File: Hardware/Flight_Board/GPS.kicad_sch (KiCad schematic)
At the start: 7 parts, among them U5 CAM-M8Q-0

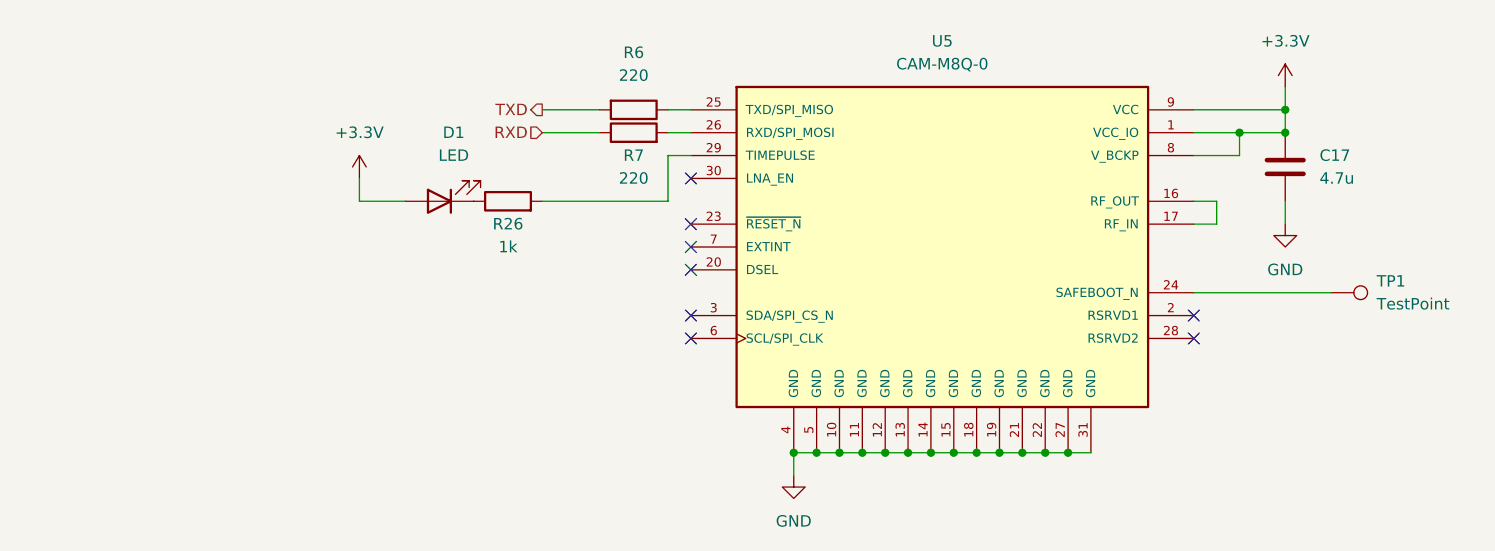
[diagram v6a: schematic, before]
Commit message: Add LEDs and test points
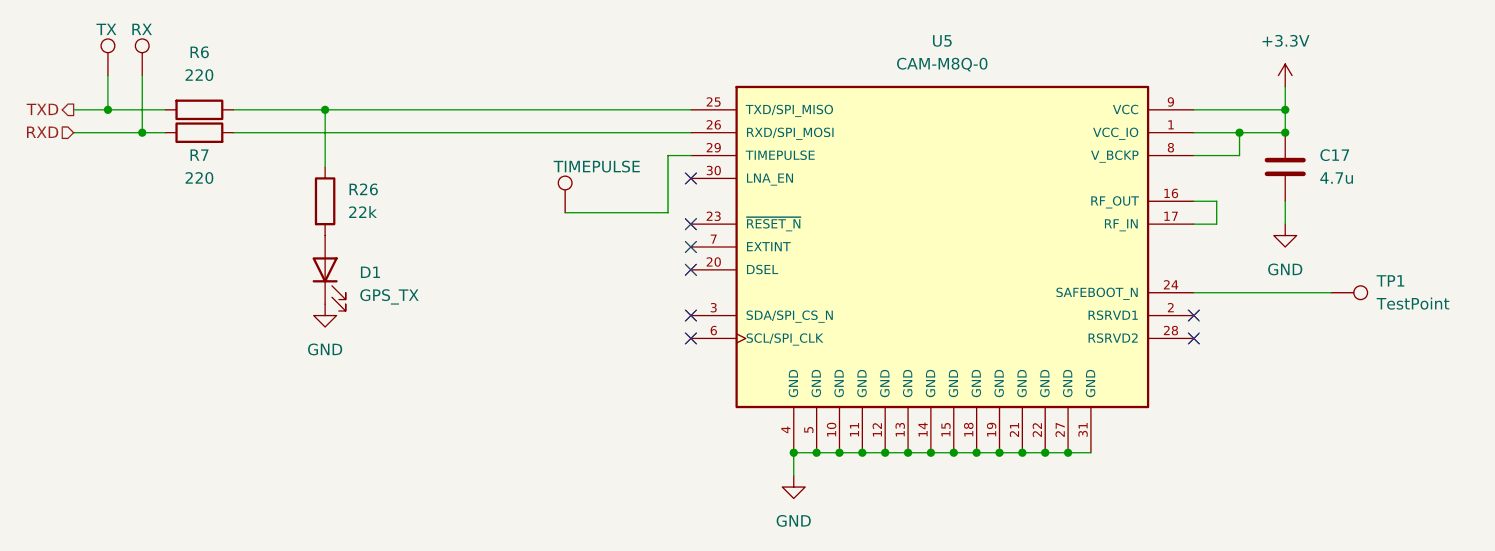
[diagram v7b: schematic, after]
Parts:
- added TP2: RX, symbol Connector:TestPoint
- added TP2: TIMEPULSE, symbol Connector:TestPoint
- added TP2: TX, symbol Connector:TestPoint
- D1: value LED -> GPS_TX
- R26: value 1k -> 22k
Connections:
- net +3.3V: no longer D1.2 (A)
- net GND: now also D1.1 (K)
- net RXD: now also TP2.1
- net TXD: now also TP2.1
- net at R26.1: now also R6.1, U5.25 (TXD/SPI_MISO); no longer D1.1 (K)
- net at U5.29 (TIMEPULSE): now also TP2.1; no longer R26.2
- new net: D1.2 (A), R26.2
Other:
- moved on the sheet: R6, R7

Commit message: final touches, bom, footprints
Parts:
- C17: footprint (none) -> Capacitor_SMD:C_0603_1608Metric_Pad1.08x0.95mm_HandSolder
- D1: footprint (none) -> LED_SMD:LED_0603_1608Metric_Pad1.05x0.95mm_HandSolder
- R26, R6, R7: footprint (none) -> Resistor_SMD:R_0603_1608Metric_Pad0.98x0.95mm_HandSolder
- TP1: value TestPoint -> SAFEBOOT; footprint (none) -> TestPoint:TestPoint_Pad_D1.0mm
- TP2: footprint (none) -> TestPoint:TestPoint_THTPad_2.0x2.0mm_Drill1.0mm
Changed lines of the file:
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@@
       (effects (font (size 1.27 1.27)))
     )
-    (property "Footprint" "" (at 91.44 60.452 90)
+    (property "Footprint" "Resistor_SMD:R_0603_1608Metric_Pad0.98x0.95mm_HandSolder" (at 91.44 60.452 90)
       (effects (font (size 1.27 1.27)) hide)
     )
@@
       (effects (font (size 1.27 1.27)) (justify left))
     )
-    (property "Footprint" "" (at 213.0552 72.39 0)
+    (property "Footprint" "Capacitor_SMD:C_0603_1608Metric_Pad1.08x0.95mm_HandSolder" (at 213.0552 72.39 0)
       (effects (font (size 1.27 1.27)) hide)
     )
@@
       (effects (font (size 1.27 1.27)))
     )
-    (property "Footprint" "" (at 91.44 66.548 90)
+    (property "Footprint" "Resistor_SMD:R_0603_1608Metric_Pad0.98x0.95mm_HandSolder" (at 91.44 66.548 90)
       (effects (font (size 1.27 1.27)) hide)
     )
@@
       (effects (font (size 1.27 1.27)) (justify left))
     )
-    (property "Footprint" "" (at 90.17 58.42 0)
+    (property "Footprint" "TestPoint:TestPoint_THTPad_2.0x2.0mm_Drill1.0mm" (at 90.17 58.42 0)
       (effects (font (size 1.27 1.27)) hide)
     )
@@
       (effects (font (size 1.27 1.27)) (justify left))
     )
-    (property "Footprint" "" (at 137.16 73.66 0)
+    (property "Footprint" "TestPoint:TestPoint_THTPad_2.0x2.0mm_Drill1.0mm" (at 137.16 73.66 0)
       (effects (font (size 1.27 1.27)) hide)
     )
@@
       (effects (font (size 1.27 1.27)) (justify left))
     )
-    (property "Footprint" "" (at 103.632 72.39 90)
+    (property "Footprint" "Resistor_SMD:R_0603_1608Metric_Pad0.98x0.95mm_HandSolder" (at 103.632 72.39 90)
       (effects (font (size 1.27 1.27)) hide)
     )
@@
     (in_bom yes) (on_board yes) (dnp no) (fields_autoplaced)
     (property "Reference" "TP1" (at 222.25 81.28 90)
-      (effects (font (size 1.27 1.27)) (justify left))
-    )
-    (property "Value" "TestPoint" (at 222.25 83.82 90)
-      (effects (font (size 1.27 1.27)) (justify left))
-    )
-    (property "Footprint" "" (at 217.17 87.63 0)
+      (effects (font (size 1.27 1.27)) (justify left) hide)
+    )
+    (property "Value" "SAFEBOOT" (at 222.25 82.55 90)
+      (effects (font (size 1.27 1.27)) (justify left))
+    )
+    (property "Footprint" "TestPoint:TestPoint_Pad_D1.0mm" (at 217.17 87.63 0)
       (effects (font (size 1.27 1.27)) hide)
     )
@@
       (effects (font (size 1.27 1.27)) (justify right))
     )
-    (property "Footprint" "" (at 105.41 80.01 0)
+    (property "Footprint" "LED_SMD:LED_0603_1608Metric_Pad1.05x0.95mm_HandSolder" (at 105.41 80.01 0)
       (effects (font (size 1.27 1.27)) hide)
     )
@@
       (effects (font (size 1.27 1.27)) (justify left))
     )
-    (property "Footprint" "" (at 86.36 58.42 0)
-      (effects (font (size 1.27 1.27)) hide)
-    )
+    (property "Footprint" "TestPoint:TestPoint_THTPad_2.0x2.0mm_Drill1.0mm" (at 86.36 58.42 0)
+      (effects (font (size 1.27 1.27)) hide)
+    )
